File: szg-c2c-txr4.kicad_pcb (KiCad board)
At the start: 6 copper layers, 50 x 35 mm, 40 parts, among them J1 SYZYGY_TXR-4, J2 SYZYGY_TXR-4, J3 Conn_01x02_Pin, U1 DSC557-0333

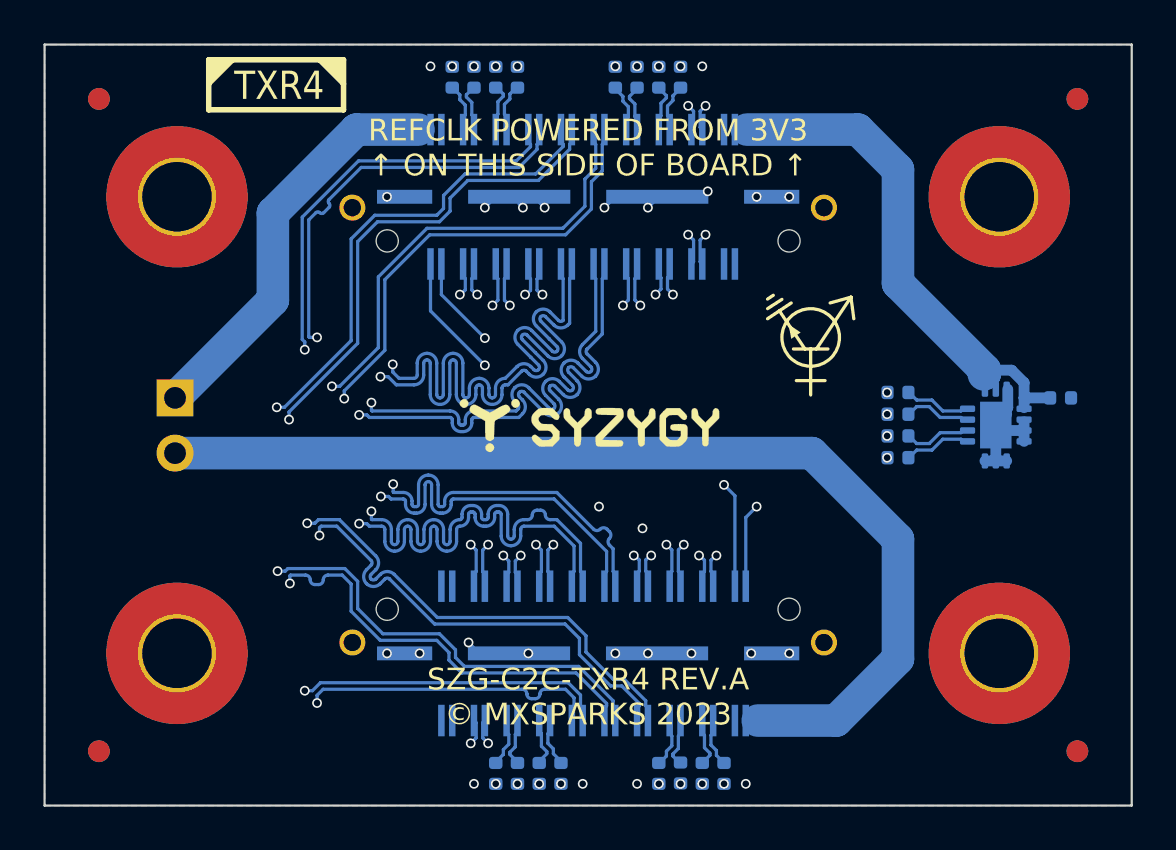
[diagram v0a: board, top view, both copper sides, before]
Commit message: change REFCLK circuit due to parts availability
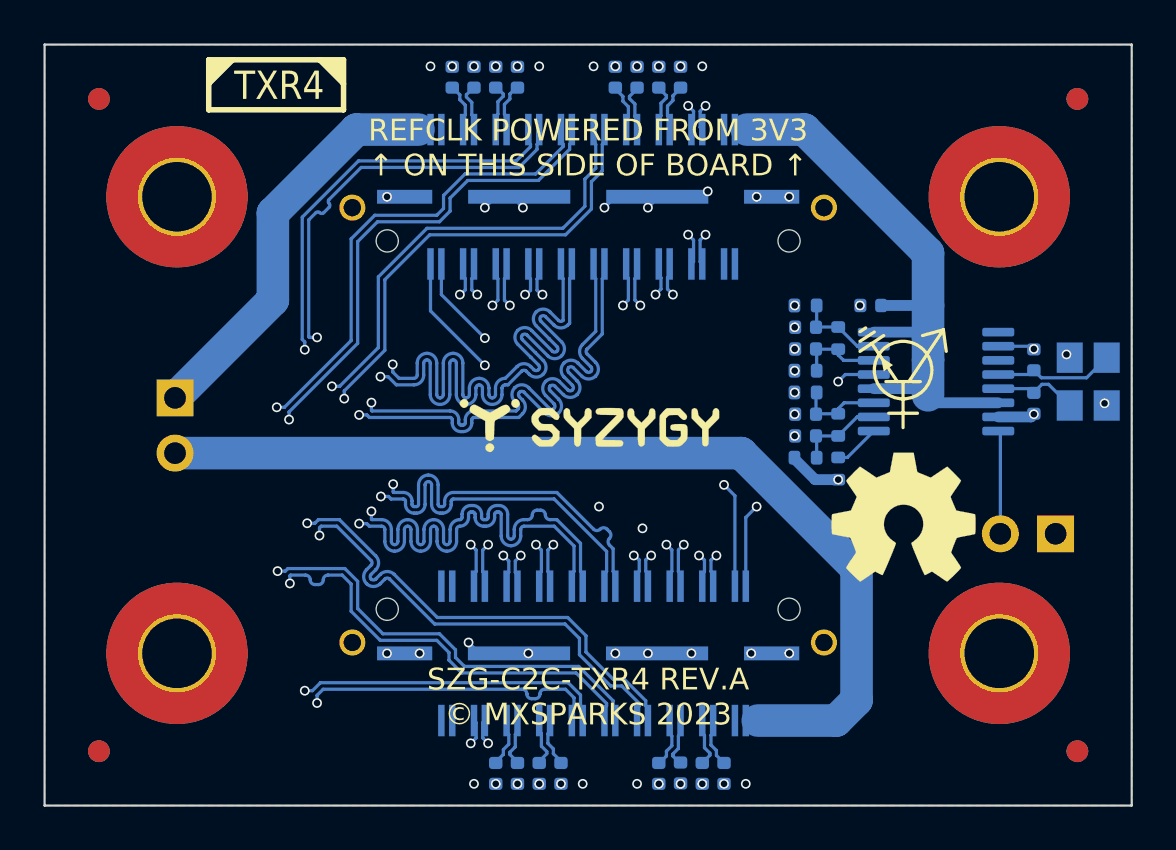
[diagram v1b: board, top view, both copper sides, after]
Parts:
- added C22: 8pF, Capacitor_SMD:C_0402_1005Metric, B.Cu at (172.5, 106.5)
- added C23: 8pF, Capacitor_SMD:C_0402_1005Metric, B.Cu at (172.5, 108.5)
- added J4: Conn_01x02_Pin, Connector_PinHeader_2.54mm:PinHeader_1x02_P2.54mm_Vertical, B.Cu at (173.5, 114.5)
- added R1: 100Ω, Resistor_SMD:R_0402_1005Metric, B.Cu at (163.5, 105.5)
- added R2: 150Ω, Resistor_SMD:R_0402_1005Metric, B.Cu at (162.0, 104.0)
- added R3: 150Ω, Resistor_SMD:R_0402_1005Metric, B.Cu at (162.0, 107.0)
- added R4: 100Ω, Resistor_SMD:R_0402_1005Metric, B.Cu at (163.5, 109.5)
- added R5: 150Ω, Resistor_SMD:R_0402_1005Metric, B.Cu at (162.0, 108.0)
- added R6: 150Ω, Resistor_SMD:R_0402_1005Metric, B.Cu at (162.0, 111.0)
- added R7: 470Ω, Resistor_SMD:R_0402_1005Metric, B.Cu at (163.5, 111.5)
- added REF**: OSHW-Symbol_6.7x6mm_SilkScreen, Symbol:OSHW-Symbol_6.7x6mm_SilkScreen, F.Cu at (166.5, 113.8)
- added Y1: 25MHz 12pF, Crystal:Crystal_SMD_3225-4Pin_3.2x2.5mm, B.Cu at (175.0, 107.5)
- C17: value 100nF -> 10nF
- U1: value DSC557-0333 -> PI6C557-03; footprint szg-c2c-txr4:VQFN14-2.5x3.2x0.9mm-EP1.4x2.1mm -> Package_SO:TSSOP-16_4.4x5mm_P0.65mm
- moved C17 9.71 mm to (165.0, 104.0), turned to 0 degrees
- moved C18 5.20 mm to (162.0, 105.0)
- moved C19 5.20 mm to (162.0, 106.0)
- moved G** 4.51 mm to (166.5, 107.0)
- moved C20 4.37 mm to (162.0, 109.0)
- moved C21 4.37 mm to (162.0, 110.0)
- moved U1 3.40 mm to (168.0, 107.5)
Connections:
- C18 pad 2: /J1_REFCLK- -> /J1_REFCLK+
- C19 pad 2: /J1_REFCLK+ -> /J1_REFCLK-
- C20 pad 1: /CLK1- -> /CLK1+
- C21 pad 1: /CLK1+ -> /CLK1-
- U1 pad 1: +3V3 -> unconnected-(U1-S0-Pad1)
- U1 pad 10: /CLK0- -> /CLK1-
- U1 pad 11: /CLK0+ -> /CLK1+
- U1 pad 13: +3V3 -> GND
- U1 pad 14: GND -> /CLK0-
- U1 pad 3: GND -> unconnected-(U1-SS0-Pad3)
- U1 pad 4: GND -> /X1
- U1 pad 5: GND -> /X2
- U1 pad 6: GND -> +3V3
- U1 pad 8: /CLK1+ -> /SS1
- U1 pad 9: /CLK1- -> /IREF
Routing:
- net /X1: track 0.00 -> 6.01 mm
- net +3V3: track 23.2 -> 28.0 mm
- net /J2_REFCLK-: track 22.0 -> 17.2 mm
- net /J2_REFCLK+: track 21.9 -> 17.2 mm
- net /SS1: track 0.00 -> 4.77 mm
- net /X2: track 0.00 -> 4.36 mm
- net /J1_REFCLK-: track 21.7 -> 17.5 mm
- net /J1_REFCLK+: track 21.7 -> 17.6 mm
- net /J2_5V: track 48.0 -> 44.5 mm
- net /IREF: track 0.00 -> 2.14 mm
- net /CLK0-: track 2.88 -> 4.04 mm
- net /CLK0+: track 2.88 -> 4.04 mm
- net /CLK1-: track 2.88 -> 4.03 mm
- net /CLK1+: track 2.88 -> 4.02 mm
- net GND: track 10.6 -> 11.7 mm, vias 26 -> 37
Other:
- board text added: "SSC EN"
